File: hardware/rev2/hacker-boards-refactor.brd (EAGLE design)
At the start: 25.4 x 58.4 mm, 38 parts, among them J1 MICRO_USB_B_JST_MC5BR3-M404-4S

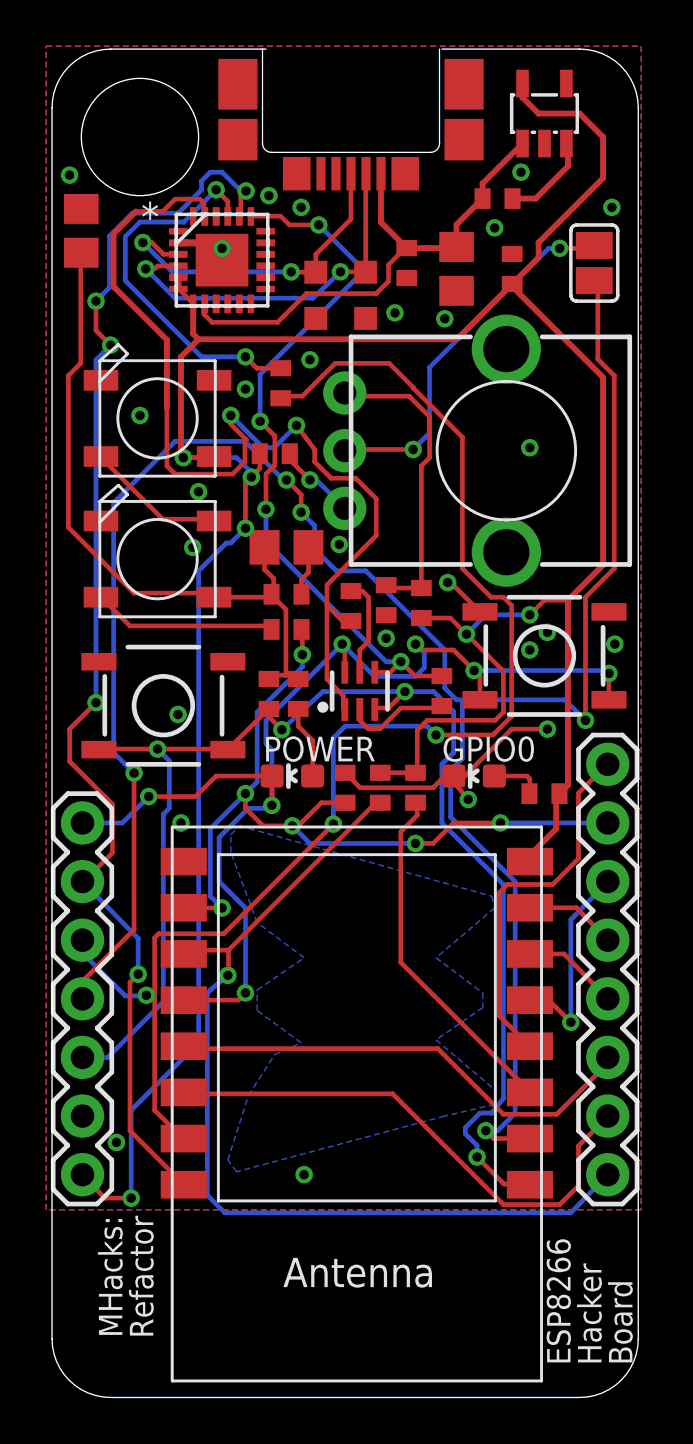
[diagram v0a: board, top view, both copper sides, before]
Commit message: Tweaked traces to make polygons better
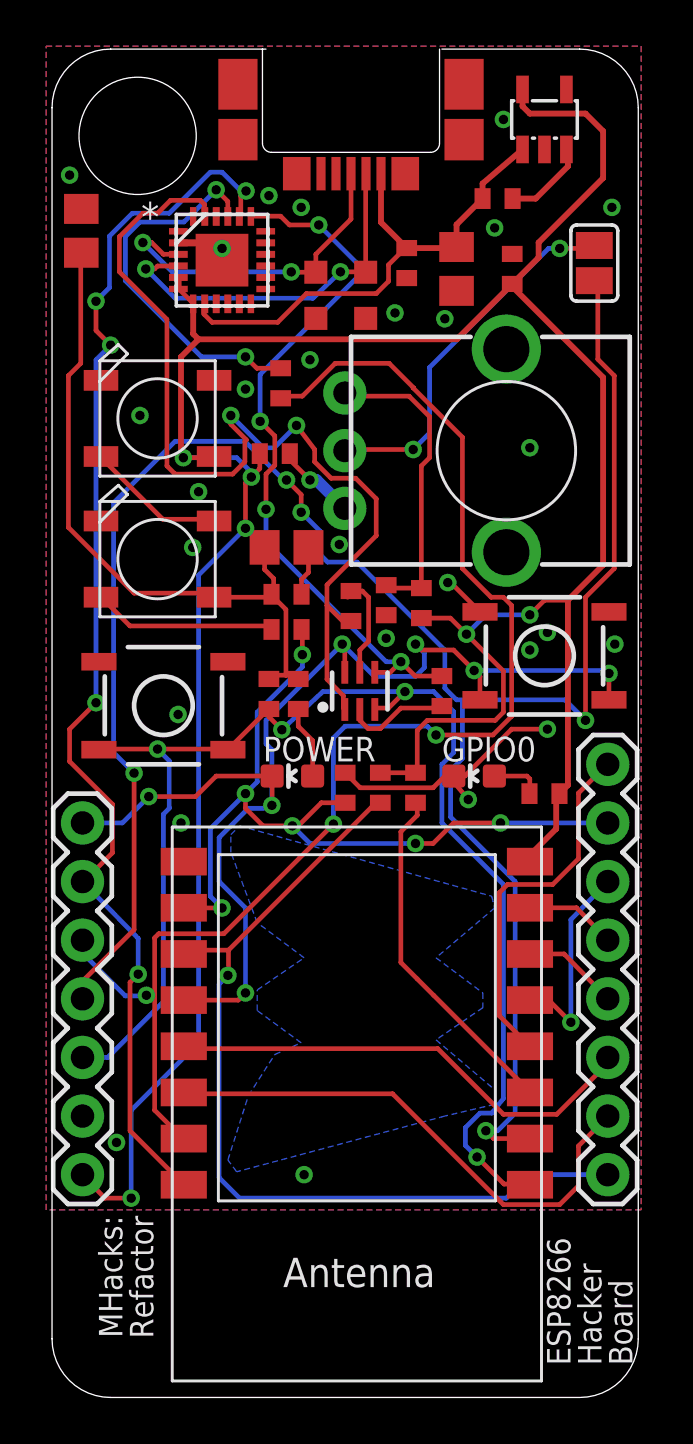
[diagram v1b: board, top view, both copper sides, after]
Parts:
- moved U$2 0.25 mm to (21.3, 55.4)
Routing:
- net GPIO2: track 40.8 -> 39.0 mm

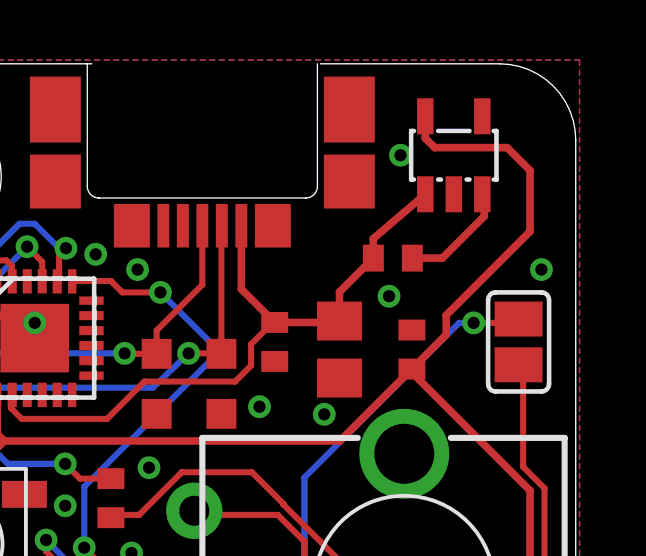
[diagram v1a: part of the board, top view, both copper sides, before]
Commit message: More polygon optimization
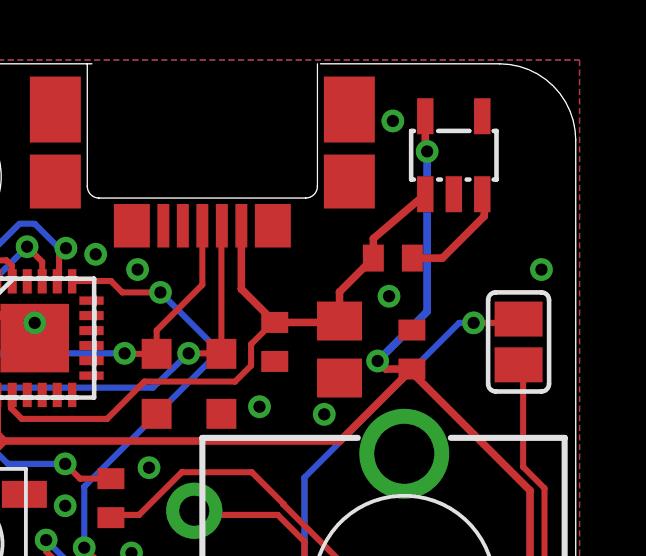
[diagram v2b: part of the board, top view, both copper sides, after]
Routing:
- net +3V3: track 156.1 -> 153.3 mm, vias 6 -> 8
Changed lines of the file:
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@@
 <layers>
 <layer number="1" name="Top" color="4" fill="1" visible="yes" active="yes"/>
-<layer number="16" name="Bottom" color="1" fill="1" visible="yes" active="yes"/>
+<layer number="16" name="Bottom" color="1" fill="1" visible="no" active="yes"/>
 <layer number="17" name="Pads" color="2" fill="1" visible="yes" active="yes"/>
 <layer number="18" name="Vias" color="2" fill="1" visible="yes" active="yes"/>
@@
 <contactref element="C7" pad="1"/>
 <contactref element="JP3" pad="7"/>
-<wire x1="23.876" y1="54.864" x2="23.876" y2="52.832" width="0.254" layer="1"/>
-<wire x1="23.876" y1="52.832" x2="21.082" y2="50.038" width="0.254" layer="1"/>
-<wire x1="21.082" y1="50.038" x2="21.082" y2="49.388" width="0.254" layer="1"/>
-<wire x1="21.082" y1="49.388" x2="19.939" y2="48.245" width="0.254" layer="1"/>
 <wire x1="19.939" y1="48.245" x2="19.939" y2="48.133" width="0.254" layer="1"/>
 <wire x1="19.939" y1="48.133" x2="23.876" y2="44.196" width="0.254" layer="1"/>
@@
 <wire x1="8.382" y1="37.658" x2="6.35" y2="35.626" width="0.2032" layer="16"/>
 <wire x1="6.35" y1="35.626" x2="6.35" y2="15.367" width="0.2032" layer="16"/>
-<wire x1="20.386" y1="55.941" x2="20.386" y2="56.672" width="0.254" layer="1"/>
-<wire x1="23.876" y1="54.864" x2="23.114" y2="55.626" width="0.254" layer="1"/>
-<wire x1="23.114" y1="55.626" x2="20.701" y2="55.626" width="0.254" layer="1"/>
-<wire x1="20.701" y1="55.626" x2="20.386" y2="55.941" width="0.254" layer="1"/>
+<wire x1="20.386" y1="55.687" x2="20.386" y2="56.672" width="0.254" layer="1"/>
+<wire x1="20.386" y1="55.687" x2="20.447" y2="55.499" width="0.254" layer="1"/>
+<via x="20.447" y="55.499" extent="1-16" drill="0.4064"/>
+<wire x1="20.447" y1="55.499" x2="20.447" y2="50.165" width="0.254" layer="16"/>
+<wire x1="20.447" y1="50.165" x2="18.796" y2="48.514" width="0.254" layer="16"/>
+<via x="18.796" y="48.514" extent="1-16" drill="0.4064"/>
+<wire x1="18.796" y1="48.514" x2="19.065" y2="48.245" width="0.254" layer="1"/>
+<wire x1="19.065" y1="48.245" x2="19.939" y2="48.245" width="0.254" layer="1"/>
 </signal>
 <signal name="GND">
@@
 <vertex x="-0.254" y="8.128"/>
 </polygon>
-<via x="19.558" y="55.372" extent="1-16" drill="0.4064"/>
+<via x="19.304" y="56.515" extent="1-16" drill="0.4064"/>
 <via x="19.177" y="50.673" extent="1-16" drill="0.4064"/>
 <via x="21.463" y="28.956" extent="1-16" drill="0.4064"/>
